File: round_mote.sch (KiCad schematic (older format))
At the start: 38 parts, among them P1 RST-GND, P10 A4 A5, P11 3.3V 5V, P12 GND RAW, P2 D1 D0, P3 D3 D2, P4 D5 D4, P5 D8 D9, P6 D10 D11, P7 D12 D13, P8 A0 A1, P9 A2 A3, U1 ATMEGA168, U2 XBEE-1B3, U3 3.3V Reg, U4 5V Reg

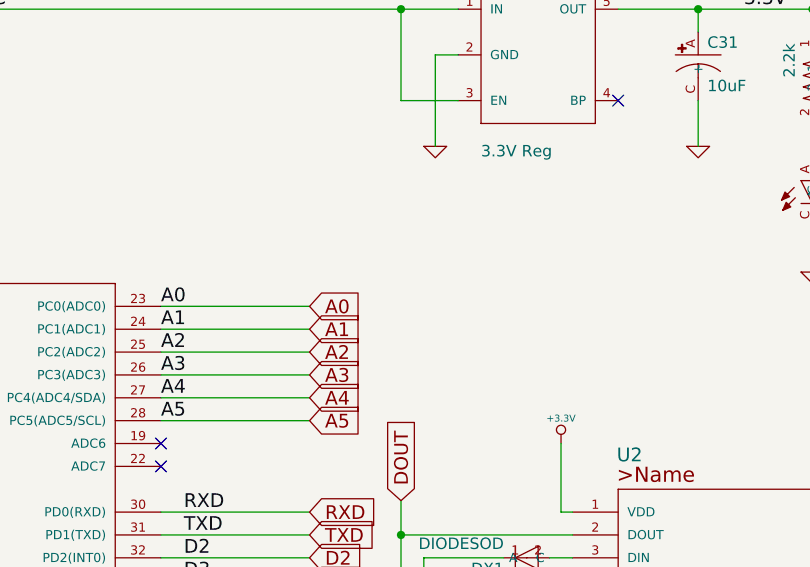
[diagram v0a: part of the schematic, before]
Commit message: Added solder jumper
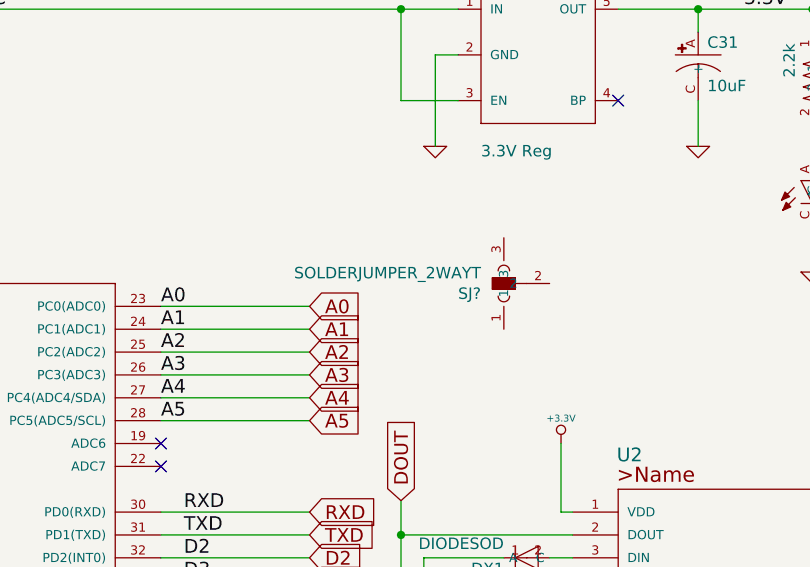
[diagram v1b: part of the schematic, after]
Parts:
- added SJ?: SOLDERJUMPER_2WAYT, SparkFun-SJ_2, symbol SOLDERJUMPER_2WAYT
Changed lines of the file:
@@
-EESchema Schematic File Version 2  date Fri 22 Apr 2011 10:57:06 AM MDT
+EESchema Schematic File Version 2  date 6/16/2012 3:52:51 PM
 LIBS:SparkFun
 LIBS:power
@@
 Sheet 1 1
 Title ""
-Date "22 apr 2011"
+Date "16 jun 2012"
 Rev ""
 Comp ""
@@
 Comment4 ""
 $EndDescr
+$Comp
+L SOLDERJUMPER_2WAYT SJ?
+U 1 1 4FDCFE4B
+P 7800 2700
+F 0 "SJ?" H 7900 2715 50  0000 L BNN
+F 1 "SOLDERJUMPER_2WAYT" H 7900 2625 50  0000 L BNN
+F 2 "SparkFun-SJ_2" H 7800 2850 50  0001 C CNN
+	1    7800 2700
+	-1   0    0    1
+$EndComp
 Wire Wire Line
 	4600 6200 4600 5750

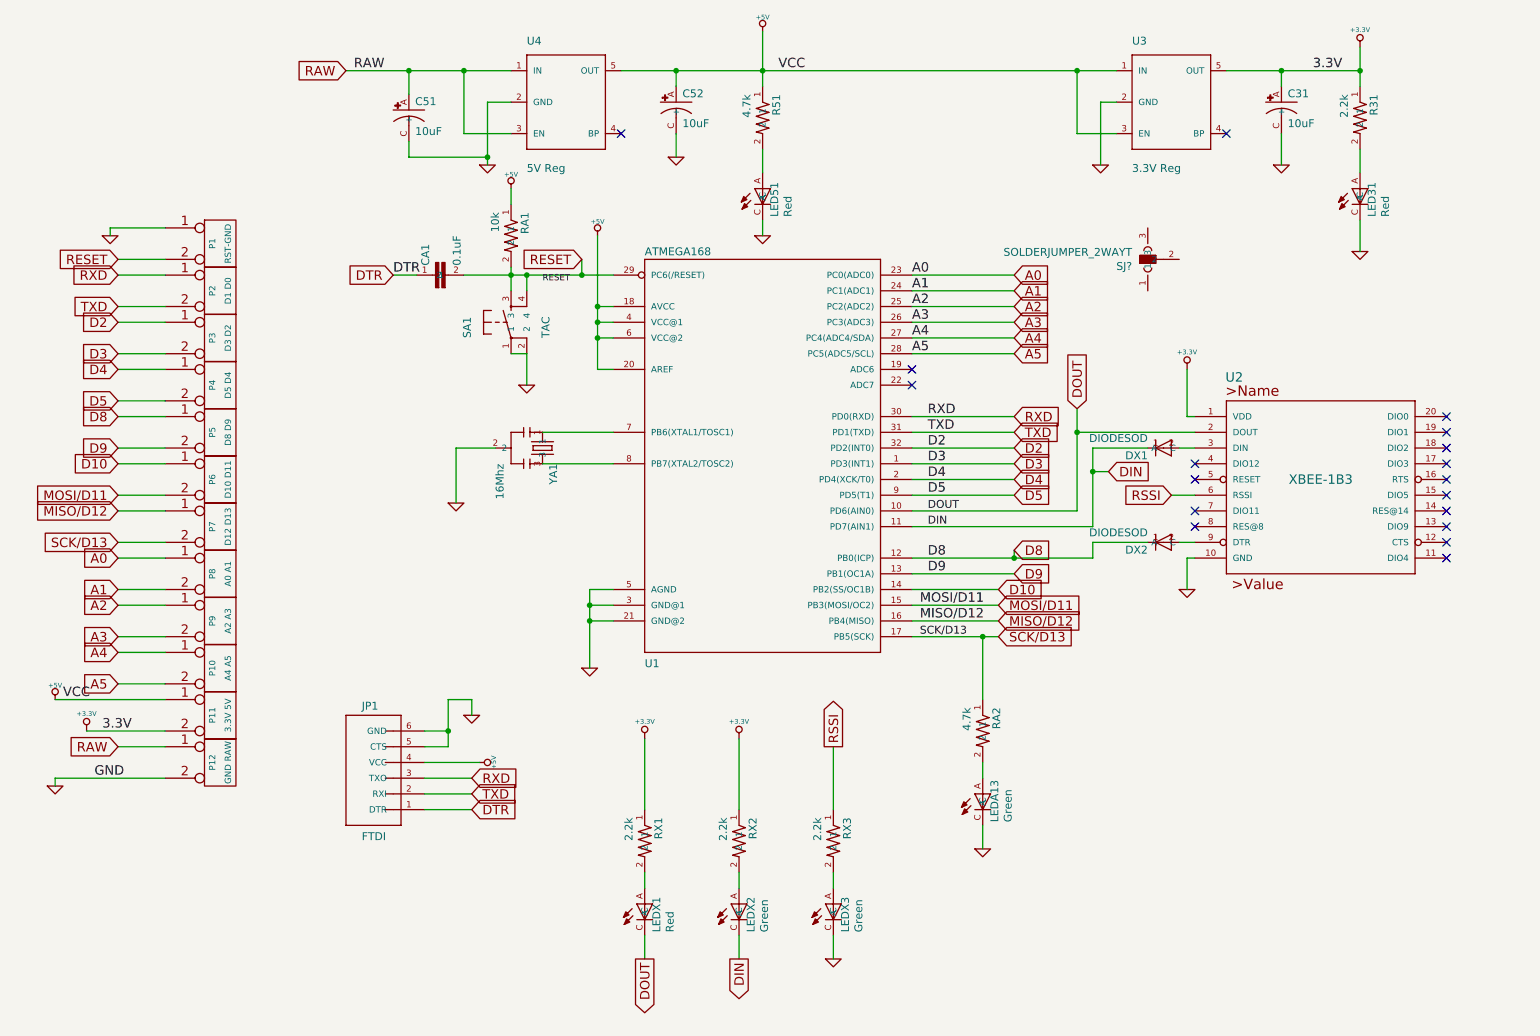
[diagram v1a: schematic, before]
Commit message: Added pullup resistor and rs485
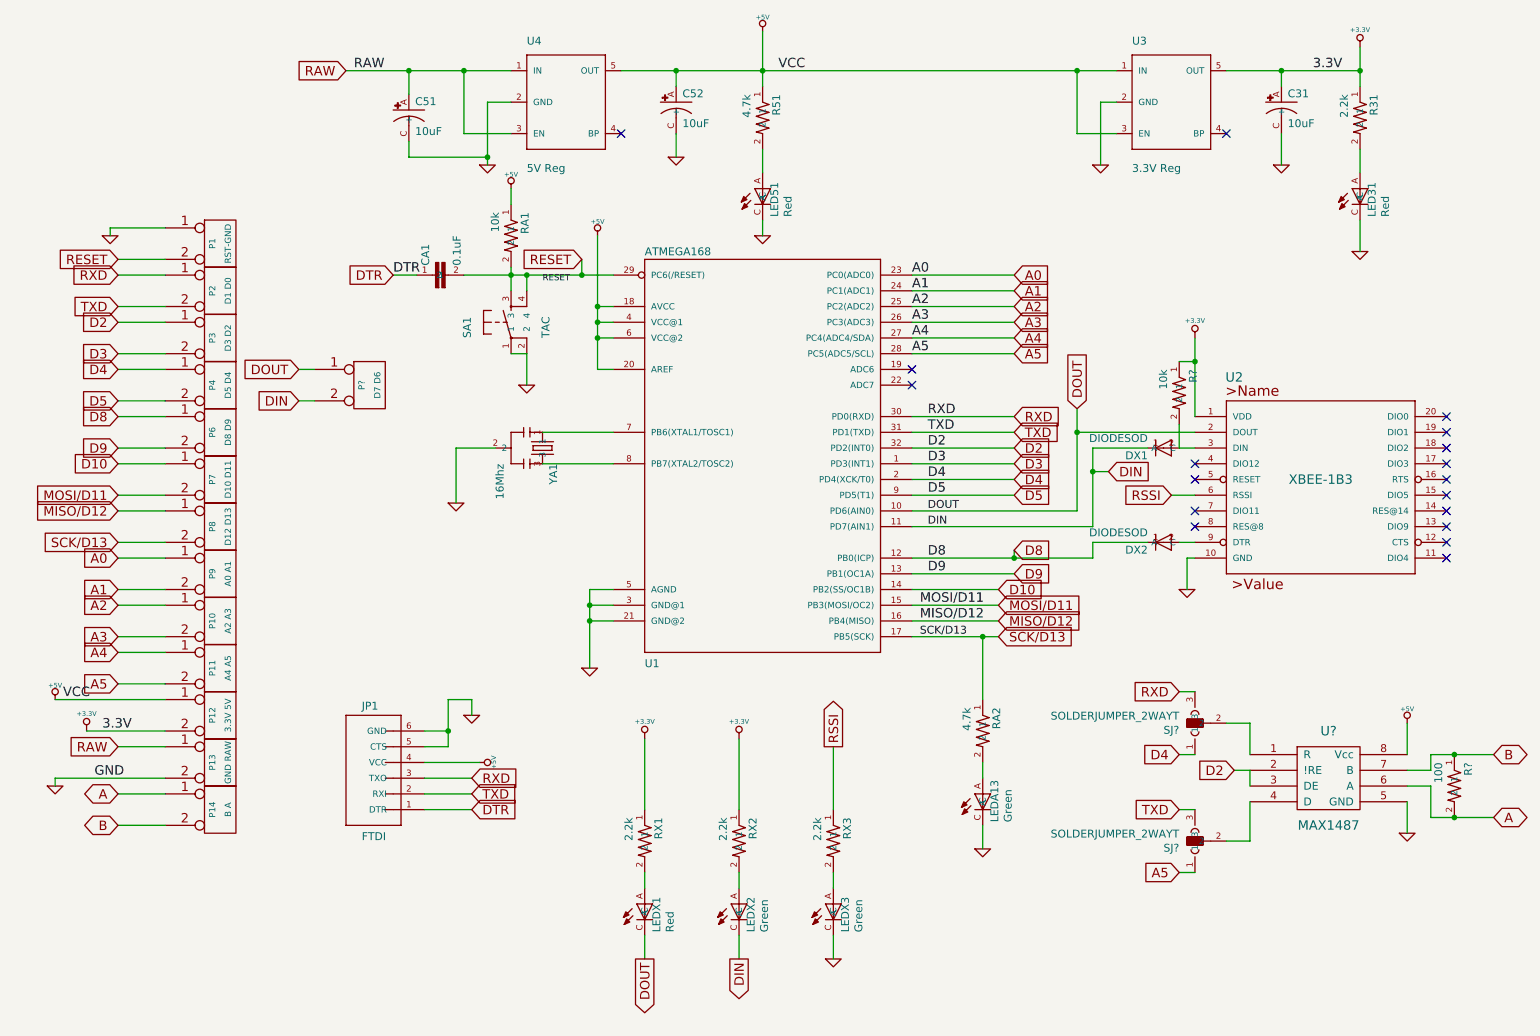
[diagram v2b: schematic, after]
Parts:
- added P14: B A, symbol CONN_2
- added P?: D7 D6, symbol CONN_2
- added R?: 100, SparkFun-0603-RES, symbol RESISTOR0603-RES
- added R?: 10k, SparkFun-0603-RES, symbol RESISTOR0603-RES
- added SJ?: SOLDERJUMPER_2WAYT, SparkFun-SJ_2, symbol SOLDERJUMPER_2WAYT
- added U?: MAX1487, symbol MAX1487
- renumbered P9 to P10, P10 to P11, P11 to P12, P12 to P13, P5 to P6, P6 to P7, P7 to P8, P8 to P9
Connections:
- net +3.3V: now also R?.1
- net +5V: now also U?.8 (Vcc)
- net A5: now also SJ?.1
- net D2: now also U?.2 (!RE), U?.3 (DE)
- net D4: now also SJ?.1
- net DIN: now also P?.2 (PM)
- net DOUT: now also P?.1 (P1)
- net GND: now also U?.5 (GND)
- net RXD: now also SJ?.3
- net TXD: now also SJ?.3
- net at DX1.2 (A), U2.3 (DIN): now also R?.2
- net at SJ?.2: now also U?.1 (R)
- new net: SJ?.2, U?.4 (D)
- new net A: P14.1 (P1), R?.2, U?.6 (A)
- new net B: P14.2 (PM), R?.1, U?.7 (B)
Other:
- moved on the sheet: SJ?

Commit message: Moved Parts arround
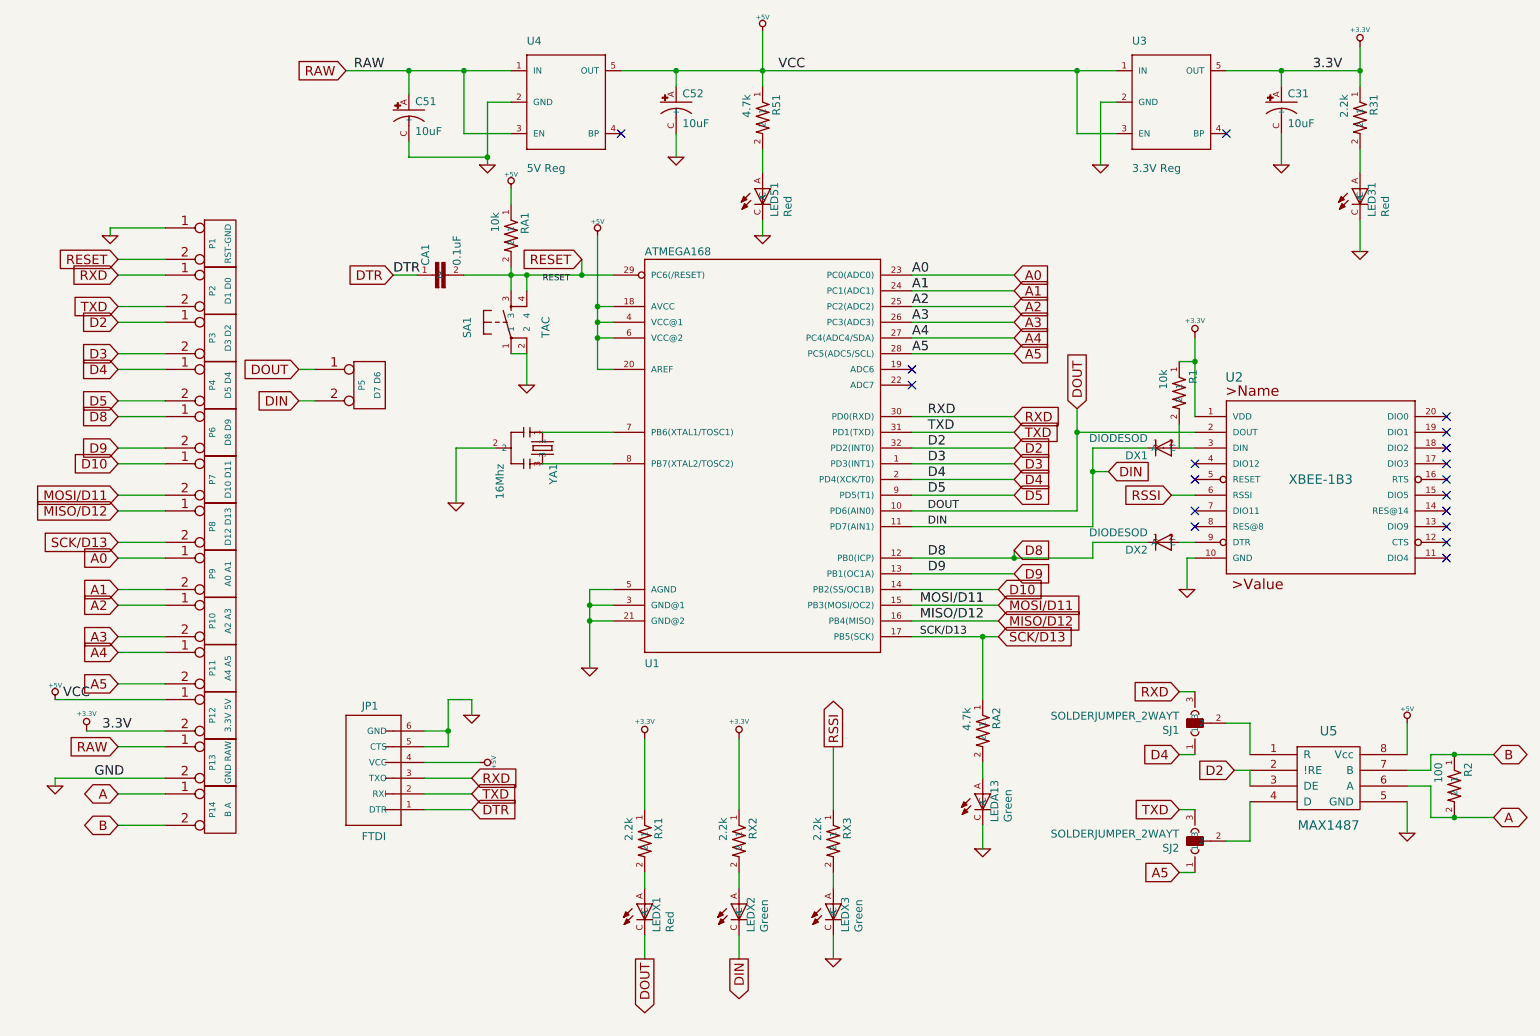
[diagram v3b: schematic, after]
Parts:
- gave numbers to parts that had none: 6
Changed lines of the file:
@@
-EESchema Schematic File Version 2  date 6/16/2012 8:29:54 PM
+EESchema Schematic File Version 2  date 6/16/2012 8:36:09 PM
 LIBS:SparkFun
 LIBS:power
@@
 DOUT
 $Comp
-L CONN_2 P?
+L CONN_2 P5
 U 1 1 4FDD4019
 P 2850 3500
-F 0 "P?" V 2800 3500 40  0000 C CNN
+F 0 "P5" V 2800 3500 40  0000 C CNN
 F 1 "D7 D6" V 2900 3500 40  0000 C CNN
 	1    2850 3500
@@
 AR Path="/4D65C2FD" Ref="R?"  Part="1"
 AR Path="/4D65C35B" Ref="R?"  Part="1"
-AR Path="/4FDD3FAF" Ref="R?"  Part="1"
-F 0 "R?" H 7850 3609 50  0000 L BNN
+AR Path="/4FDD3FAF" Ref="R1"  Part="1"
+F 0 "R1" H 7850 3609 50  0000 L BNN
 F 1 "10k" H 7850 3420 50  0000 L BNN
 F 2 "SparkFun-0603-RES" H 8000 3700 50  0001 C CNN
@@
 AR Path="/4D65C2FD" Ref="R?"  Part="1"
 AR Path="/4D65C35B" Ref="R?"  Part="1"
-AR Path="/4FDD3DC2" Ref="R?"  Part="1"
-F 0 "R?" H 9600 6109 50  0000 L BNN
+AR Path="/4FDD3DC2" Ref="R2"  Part="1"
+F 0 "R2" H 9600 6109 50  0000 L BNN
 F 1 "100" H 9600 5920 50  0000 L BNN
 F 2 "SparkFun-0603-RES" H 9750 6200 50  0001 C CNN
@@
 RXD
 $Comp
-L GND #PWR?
+L GND #PWR01
 U 1 1 4FDD0363
 P 9450 6350
-F 0 "#PWR?" H 9450 6350 30  0001 C CNN
+F 0 "#PWR01" H 9450 6350 30  0001 C CNN
 F 1 "GND" H 9450 6280 30  0001 C CNN
 	1    9450 6350
@@
 $EndComp
 $Comp
-L +5V #PWR?
+L +5V #PWR02
 U 1 1 4FDD0352
 P 9450 5650
-F 0 "#PWR?" H 9450 5740 20  0001 C CNN
+F 0 "#PWR02" H 9450 5740 20  0001 C CNN
 F 1 "+5V" H 9450 5740 30  0000 C CNN
 	1    9450 5650
@@
 P 8100 6400
 AR Path="/4FDCFE4B" Ref="SJ?"  Part="1"
-AR Path="/4FDD0326" Ref="SJ?"  Part="1"
-F 0 "SJ?" H 8200 6415 50  0000 L BNN
+AR Path="/4FDD0326" Ref="SJ2"  Part="1"
+F 0 "SJ2" H 8200 6415 50  0000 L BNN
 F 1 "SOLDERJUMPER_2WAYT" H 8200 6325 50  0000 L BNN
 F 2 "SparkFun-SJ_2" H 8100 6550 50  0001 C CNN
@@
 $EndComp
 $Comp
-L MAX1487 U?
+L MAX1487 U5
 U 1 1 4FDD0317
 P 8950 6000
-F 0 "U?" H 8950 6300 60  0000 C CNN
+F 0 "U5" H 8950 6300 60  0000 C CNN
 F 1 "MAX1487" H 8950 5700 60  0000 C CNN
 	1    8950 6000
@@
 $EndComp
 $Comp
-L SOLDERJUMPER_2WAYT SJ?
+L SOLDERJUMPER_2WAYT SJ1
 U 1 1 4FDCFE4B
 P 8100 5650
-F 0 "SJ?" H 8200 5665 50  0000 L BNN
+F 0 "SJ1" H 8200 5665 50  0000 L BNN
 F 1 "SOLDERJUMPER_2WAYT" H 8200 5575 50  0000 L BNN
 F 2 "SparkFun-SJ_2" H 8100 5800 50  0001 C CNN
@@
 $EndComp
 $Comp
-L +3.3V #PWR01
+L +3.3V #PWR03
 U 1 1 4DB1A254
 P 4600 5750
-F 0 "#PWR01" H 4600 5710 30  0001 C CNN
+F 0 "#PWR03" H 4600 5710 30  0001 C CNN
 F 1 "+3.3V" H 4600 5860 30  0000 C CNN
 	1    4600 5750
@@
 $EndComp
 $Comp
-L +3.3V #PWR02
+L +3.3V #PWR04
 U 1 1 4DB1A201
 P 9150 1350
-F 0 "#PWR02" H 9150 1310 30  0001 C CNN
+F 0 "#PWR04" H 9150 1310 30  0001 C CNN
 F 1 "+3.3V" H 9150 1460 30  0000 C CNN
 	1    9150 1350
@@
 NoConn ~ 4450 1900
 $Comp
-L +3.3V #PWR03
+L +3.3V #PWR05
 U 1 1 4DB0FAA5
 P 5200 5750
-F 0 "#PWR03" H 5200 5710 30  0001 C CNN
+F 0 "#PWR05" H 5200 5710 30  0001 C CNN
 F 1 "+3.3V" H 5200 5860 30  0000 C CNN
 	1    5200 5750
@@
 RSSI
 $Comp
-L GND #PWR04
+L GND #PWR06
 U 1 1 4DB0F978
 P 5800 7150
-F 0 "#PWR04" H 5800 7150 30  0001 C CNN
+F 0 "#PWR06" H 5800 7150 30  0001 C CNN
 F 1 "GND" H 5800 7080 30  0001 C CNN
 	1    5800 7150
@@
 A4
 $Comp
-L +5V #PWR05
+L +5V #PWR07
 U 1 1 4DAF7441
 P 5350 1250
-F 0 "#PWR05" H 5350 1340 20  0001 C CNN
+F 0 "#PWR07" H 5350 1340 20  0001 C CNN
 F 1 "+5V" H 5350 1340 30  0000 C CNN
 	1    5350 1250
@@
 $EndComp
 $Comp
-L +5V #PWR06
+L +5V #PWR08
 U 1 1 4DAF73F4
 P 3750 2250
-F 0 "#PWR06" H 3750 2340 20  0001 C CNN
+F 0 "#PWR08" H 3750 2340 20  0001 C CNN
 F 1 "+5V" H 3750 2340 30  0000 C CNN
 	1    3750 2250
@@
 $EndComp
 $Comp
-L GND #PWR07
+L GND #PWR09
 U 1 1 4DAF73BB
 P 9150 2650
-F 0 "#PWR07" H 9150 2650 30  0001 C CNN
+F 0 "#PWR09" H 9150 2650 30  0001 C CNN
 F 1 "GND" H 9150 2580 30  0001 C CNN
 	1    9150 2650
@@
 D10
 $Comp
-L +3.3V #PWR08
+L +3.3V #PWR010
 U 1 1 4DAD132F
 P 1050 5700
-F 0 "#PWR08" H 1050 5660 30  0001 C CNN
+F 0 "#PWR010" H 1050 5660 30  0001 C CNN
 F 1 "+3.3V" H 1050 5810 30  0000 C CNN
 	1    1050 5700
@@
 $EndComp
 $Comp
-L +5V #PWR09
+L +5V #PWR011
 U 1 1 4DAD1328
 P 850 5500
-F 0 "#PWR09" H 850 5590 20  0001 C CNN
+F 0 "#PWR011" H 850 5590 20  0001 C CNN
 F 1 "+5V" H 850 5590 30  0000 C CNN
 	1    850  5500
@@
 $EndComp
 $Comp
-L GND #PWR010
+L GND #PWR012
 U 1 1 4DAD131B
 P 850 6050
-F 0 "#PWR010" H 850 6050 30  0001 C CNN
+F 0 "#PWR012" H 850 6050 30  0001 C CNN
 F 1 "GND" H 850 5980 30  0001 C CNN
 	1    850  6050
@@
 RESET
 $Comp
-L GND #PWR011
+L GND #PWR013
 U 1 1 4D6E720D
 P 1200 2550
-F 0 "#PWR011" H 1200 2550 30  0001 C CNN
+F 0 "#PWR013" H 1200 2550 30  0001 C CNN
 F 1 "GND" H 1200 2480 30  0001 C CNN
 	1    1200 2550
@@
 DTR
 $Comp
-L +5V #PWR012
+L +5V #PWR014
 U 1 1 4D6D9D12
 P 3550 5900
-F 0 "#PWR012" H 3550 5990 20  0001 C CNN
+F 0 "#PWR014" H 3550 5990 20  0001 C CNN
 F 1 "+5V" H 3550 5990 30  0000 C CNN
 	1    3550 5900
@@
 $EndComp
 $Comp
-L GND #PWR013
+L GND #PWR015
 U 1 1 4D6D9C1A
 P 3850 3500
-F 0 "#PWR013" H 3850 3500 30  0001 C CNN
+F 0 "#PWR015" H 3850 3500 30  0001 C CNN
 F 1 "GND" H 3850 3430 30  0001 C CNN
 	1    3850 3500
@@
 $EndComp
 $Comp
-L +3.3V #PWR014
+L +3.3V #PWR016
 U 1 1 4D6D941A
 P 8100 3200
-F 0 "#PWR014" H 8100 3160 30  0001 C CNN
+F 0 "#PWR016" H 8100 3160 30  0001 C CNN
 F 1 "+3.3V" H 8100 3310 30  0000 C CNN
 	1    8100 3200
@@
 $EndComp
 $Comp
-L GND #PWR015
+L GND #PWR017
 U 1 1 4D6D93A2
 P 8650 2100
-F 0 "#PWR015" H 8650 2100 30  0001 C CNN
+F 0 "#PWR017" H 8650 2100 30  0001 C CNN
 F 1 "GND" H 8650 2030 30  0001 C CNN
 	1    8650 2100
@@
 $EndComp
 $Comp
-L +5V #PWR016
+L +5V #PWR018
 U 1 1 4D6D9366
 P 4300 2550
-F 0 "#PWR016" H 4300 2640 20  0001 C CNN
+F 0 "#PWR018" H 4300 2640 20  0001 C CNN
 F 1 "+5V" H 4300 2640 30  0000 C CNN
 	1    4300 2550
@@
 VCC
 $Comp
-L GND #PWR017
+L GND #PWR019
 U 1 1 4D6D92AE
 P 5350 2550
-F 0 "#PWR017" H 5350 2550 30  0001 C CNN
+F 0 "#PWR019" H 5350 2550 30  0001 C CNN
 F 1 "GND" H 5350 2480 30  0001 C CNN
 	1    5350 2550
@@
 $EndComp
 $Comp
-L GND #PWR018
+L GND #PWR020
 U 1 1 4D6D9242
 P 4800 2050
-F 0 "#PWR018" H 4800 2050 30  0001 C CNN
+F 0 "#PWR020" H 4800 2050 30  0001 C CNN
 F 1 "GND" H 4800 1980 30  0001 C CNN
 	1    4800 2050
@@
 RAW
 $Comp
-L GND #PWR019
+L GND #PWR021
 U 1 1 4D6D9107
 P 7500 2100
-F 0 "#PWR019" H 7500 2100 30  0001 C CNN
+F 0 "#PWR021" H 7500 2100 30  0001 C CNN
 F 1 "GND" H 7500 2030 30  0001 C CNN
 	1    7500 2100
@@
 $EndComp
 $Comp
-L GND #PWR020
+L GND #PWR022
 U 1 1 4D6D90E3
 P 3600 2100
-F 0 "#PWR020" H 3600 2100 30  0001 C CNN
+F 0 "#PWR022" H 3600 2100 30  0001 C CNN
 F 1 "GND" H 3600 2030 30  0001 C CNN
 	1    3600 2100
@@
 RXD
 $Comp
-L GND #PWR021
+L GND #PWR023
 U 1 1 4D6D6CFC
 P 3500 5600
-F 0 "#PWR021" H 3500 5600 30  0001 C CNN
+F 0 "#PWR023" H 3500 5600 30  0001 C CNN
 F 1 "GND" H 3500 5530 30  0001 C CNN
 	1    3500 5600
@@
 $EndComp
 $Comp
-L GND #PWR022
+L GND #PWR024
 U 1 1 4D6D3C3E
 P 3400 4250
-F 0 "#PWR022" H 3400 4250 30  0001 C CNN
+F 0 "#PWR024" H 3400 4250 30  0001 C CNN
 F 1 "GND" H 3400 4180 30  0001 C CNN
 	1    3400 4250
@@
 $EndComp
 $Comp
-L GND #PWR023
+L GND #PWR025
 U 1 1 4D6D3811
 P 8050 4800
-F 0 "#PWR023" H 8050 4800 30  0001 C CNN
+F 0 "#PWR025" H 8050 4800 30  0001 C CNN
 F 1 "GND" H 8050 4730 30  0001 C CNN
 	1    8050 4800
@@
 $EndComp
 $Comp
-L GND #PWR024
+L GND #PWR026
 U 1 1 4D6D37F9
 P 6750 6450
-F 0 "#PWR024" H 6750 6450 30  0001 C CNN
+F 0 "#PWR026" H 6750 6450 30  0001 C CNN
 F 1 "GND" H 6750 6380 30  0001 C CNN
 	1    6750 6450
@@
 $EndComp
 $Comp
-L GND #PWR025
+L GND #PWR027
 U 1 1 4D6D37C1
 P 4250 5300
-F 0 "#PWR025" H 4250 5300 30  0001 C CNN
+F 0 "#PWR027" H 4250 5300 30  0001 C CNN
 F 1 "GND" H 4250 5230 30  0001 C CNN
 	1    4250 5300
